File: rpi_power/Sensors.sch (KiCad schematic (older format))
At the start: 14 parts, among them Q6 IRLML6344TRPBF

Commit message: Components placed.
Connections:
- net ADC1: no longer R8.1
- net ADC2: no longer R10.1
- net ADC3: no longer R12.1
- new net ADC1_IN: R8.1
- new net ADC2_IN: R10.1
- new net ADC3_IN: R12.1
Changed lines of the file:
@@
 General purpose ADCs
 Text GLabel 7050 3200 1    50   Input ~ 0
-ADC1
+ADC1_IN
 Text GLabel 8200 3200 1    50   Input ~ 0
-ADC2
+ADC2_IN
 Text GLabel 9300 3200 1    50   Input ~ 0
-ADC3
+ADC3_IN
 $EndSCHEMATC

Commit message: Routing done, pending review.
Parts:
- C12, C13, C14: footprint Capacitor_SMD:C_0805_2012Metric_Pad1.15x1.40mm_HandSolder -> Capacitor_SMD:C_0603_1608Metric_Pad1.05x0.95mm_HandSolder
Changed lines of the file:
@@
 F 0 "C12" H 7515 4146 50  0000 L CNN
 F 1 "UNKN" H 7450 4000 50  0000 L CNN
-F 2 "Capacitor_SMD:C_0805_2012Metric_Pad1.15x1.40mm_HandSolder" H 7438 3950 50  0001 C CNN
+F 2 "Capacitor_SMD:C_0603_1608Metric_Pad1.05x0.95mm_HandSolder" H 7438 3950 50  0001 C CNN
 F 3 "~" H 7400 4100 50  0001 C CNN
 	1    7400 4100
@@
 F 0 "C13" H 8665 4146 50  0000 L CNN
 F 1 "UNKN" H 8600 4000 50  0000 L CNN
-F 2 "Capacitor_SMD:C_0805_2012Metric_Pad1.15x1.40mm_HandSolder" H 8588 3950 50  0001 C CNN
+F 2 "Capacitor_SMD:C_0603_1608Metric_Pad1.05x0.95mm_HandSolder" H 8588 3950 50  0001 C CNN
 F 3 "~" H 8550 4100 50  0001 C CNN
 	1    8550 4100
@@
 F 0 "C14" H 9765 4146 50  0000 L CNN
 F 1 "UNKN" H 9700 4000 50  0000 L CNN
-F 2 "Capacitor_SMD:C_0805_2012Metric_Pad1.15x1.40mm_HandSolder" H 9688 3950 50  0001 C CNN
+F 2 "Capacitor_SMD:C_0603_1608Metric_Pad1.05x0.95mm_HandSolder" H 9688 3950 50  0001 C CNN
 F 3 "~" H 9650 4100 50  0001 C CNN
 	1    9650 4100

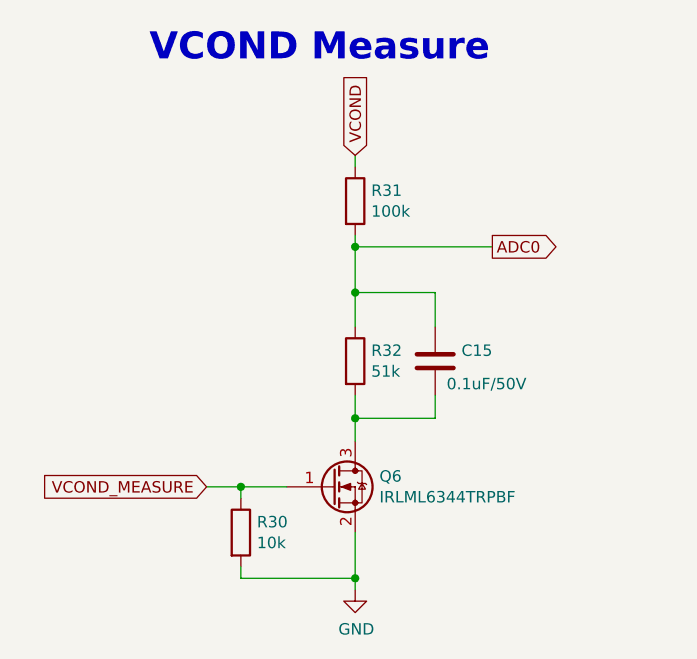
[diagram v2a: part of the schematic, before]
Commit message: Differentiated VCOND and BATT+. Routing done.
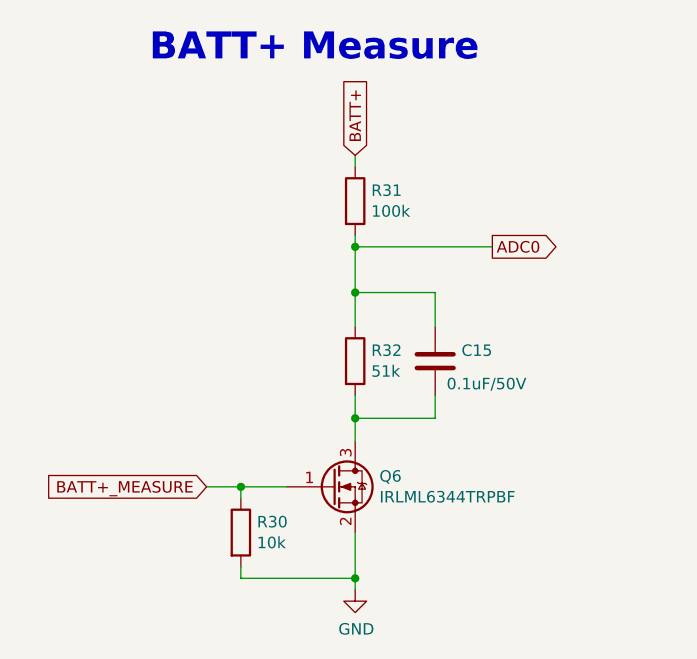
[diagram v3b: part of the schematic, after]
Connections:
- net VCOND renamed BATT+
- net VCOND_MEASURE renamed BATT+_MEASURE
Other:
- note added: "BATT+ Measure"
- note removed: "VCOND Measure"
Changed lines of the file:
@@
 Connection ~ 2750 4100
 Text Notes 1850 2550 0    118  ~ 24
-VCOND Measure
+BATT+ Measure
 Connection ~ 2750 3350
 Wire Wire Line
@@
 $EndComp
 Text GLabel 2100 4400 0    50   Input ~ 0
-VCOND_MEASURE
+BATT+_MEASURE
 Text GLabel 2750 2950 1    50   Input ~ 0
-VCOND
+BATT+
 Text GLabel 3350 3350 2    50   Output ~ 0
 ADC0
